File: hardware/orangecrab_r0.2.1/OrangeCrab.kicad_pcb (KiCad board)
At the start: 6 copper layers, 50.8 x 22.9 mm, 96 parts, among them J6 Conn_01x05, U1 TLV62569DRL, U10 NCP115-2.5, U2 TLV62569DRL, U3 LFE5U-25F-8MG285C, U4 MT41K64M16TW-107_J-TR, U6 W25Q128JVP, U7 TLV62569DRL

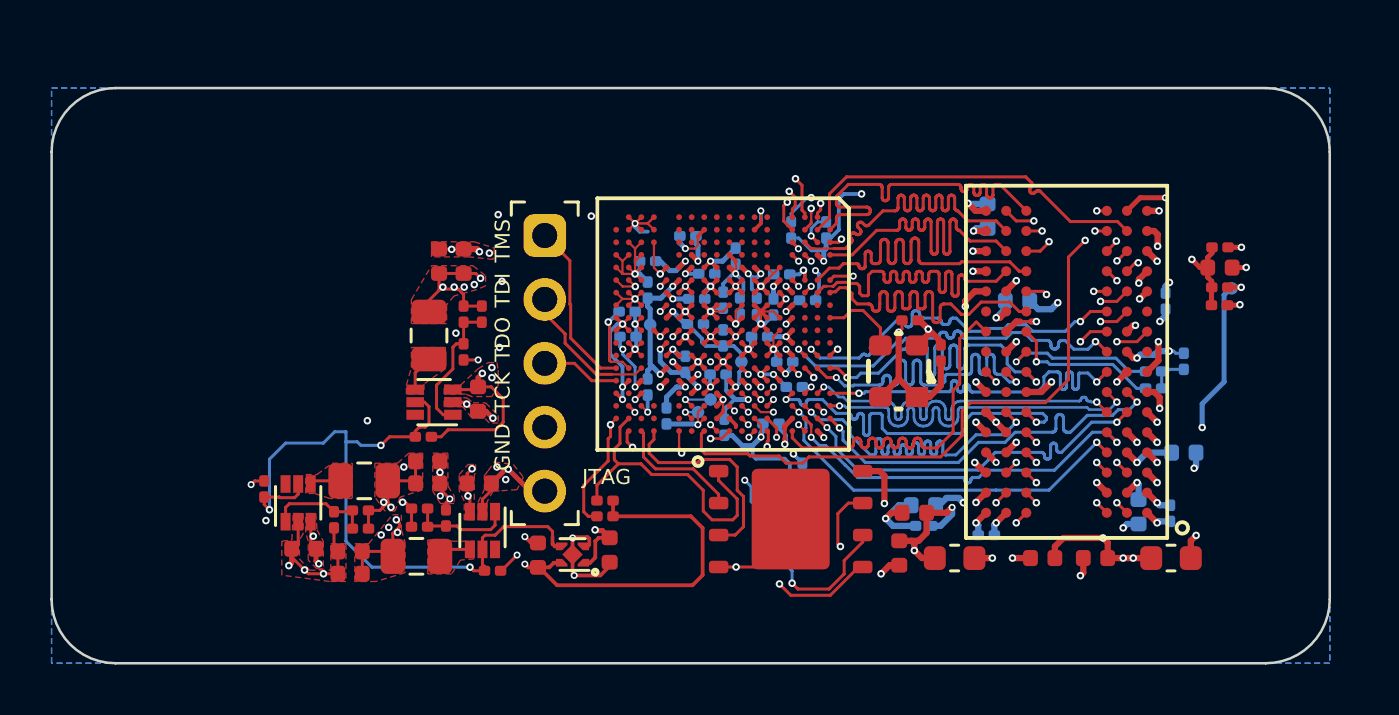
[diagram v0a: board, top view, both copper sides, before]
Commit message: M.2 form factor
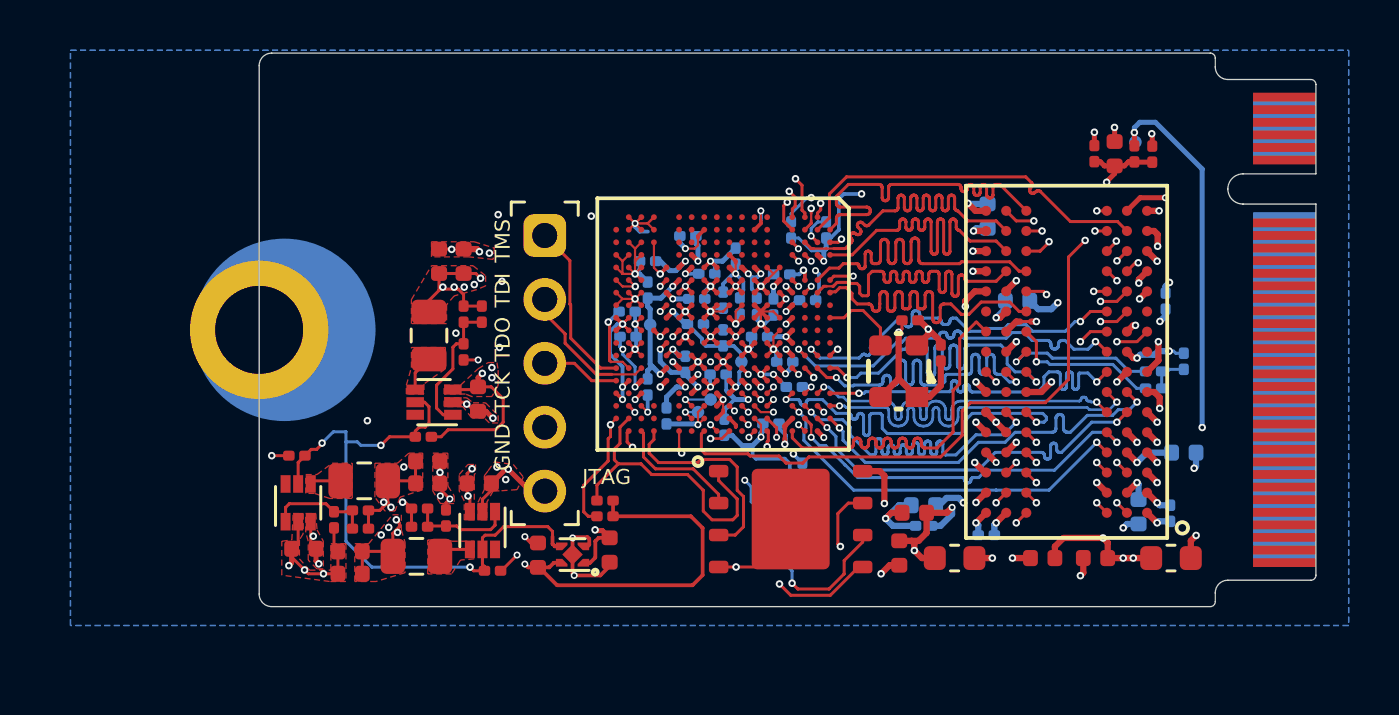
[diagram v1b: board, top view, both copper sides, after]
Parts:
- added U$1: M.2-B-KEY, M.2-Templates:M.2-B-KEY, F.Cu at (184.8, 101.1)
- moved TP31 6.96 mm to (177.6, 93.7), turned to 90 degrees
- moved R2 6.57 mm to (178.3, 94.1), turned to 90 degrees
- moved R1 6.30 mm to (177.5, 94.1), turned to -90 degrees
- moved C2 6.23 mm to (176.0, 94.1), turned to 90 degrees
- moved C3 6.16 mm to (176.8, 94.1), turned to 90 degrees
- moved R25 1.86 mm to (144.3, 106.1), turned to 180 degrees
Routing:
- net P1.35V: track 93.5 -> 101.5 mm
- net EN: track 28.7 -> 24.1 mm
- net VSYS: track 32.6 -> 29.0 mm
- net GND: vias 102 -> 101
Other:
- board size 50.8 x 22.9 mm -> 42 x 22 mm

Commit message: connect all spare IOs to M.2
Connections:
- U$1 pad MOUNTING-HOLE: unconnected-(U$1-MP1-PadMOUNTING-HOLE) -> GND
- U$1 pad P$1: unconnected-(U$1-1-PadP$1) -> GND
- U$1 pad P$10: unconnected-(U$1-10-PadP$10) -> VSYS
- U$1 pad P$11: unconnected-(U$1-11-PadP$11) -> GND
- U$1 pad P$2: unconnected-(U$1-2-PadP$2) -> VSYS
- U$1 pad P$20: unconnected-(U$1-20-PadP$20) -> 3V3_IO0_H4
- U$1 pad P$21: unconnected-(U$1-21-PadP$21) -> 3V3_IO1_G4
- U$1 pad P$22: unconnected-(U$1-22-PadP$22) -> 3V3_IO2_F4
- U$1 pad P$23: unconnected-(U$1-23-PadP$23) -> 3V3_IO3_F3
- U$1 pad P$24: unconnected-(U$1-24-PadP$24) -> 3V3_IO4_H3
- U$1 pad P$25: unconnected-(U$1-25-PadP$25) -> 3V3_IO5_G3
- U$1 pad P$26: unconnected-(U$1-26-PadP$26) -> 3V3_IO6_J3
- U$1 pad P$27: unconnected-(U$1-27-PadP$27) -> 3V3_IO7_H2
- U$1 pad P$28: unconnected-(U$1-28-PadP$28) -> 3V3_IO8_F2
- U$1 pad P$29: unconnected-(U$1-29-PadP$29) -> 3V3_IO9_G1
- U$1 pad P$3: unconnected-(U$1-3-PadP$3) -> GND
- U$1 pad P$30: unconnected-(U$1-30-PadP$30) -> 3V3_IO10_J2
- U$1 pad P$31: unconnected-(U$1-31-PadP$31) -> 3V3_IO11_J1
- U$1 pad P$32: unconnected-(U$1-32-PadP$32) -> 3V3_IO12_F1
- U$1 pad P$33: unconnected-(U$1-33-PadP$33) -> 3V3_IO13_H1
- U$1 pad P$34: unconnected-(U$1-34-PadP$34) -> 3V3_IO14_K4
- U$1 pad P$35: unconnected-(U$1-35-PadP$35) -> 3V3_IO15_L4
- U$1 pad P$36: unconnected-(U$1-36-PadP$36) -> 3V3_IO16_N4
- U$1 pad P$37: unconnected-(U$1-37-PadP$37) -> 3V3_IO17_N3
- U$1 pad P$38: unconnected-(U$1-38-PadP$38) -> 3V3_IO18_M3
- U$1 pad P$39: unconnected-(U$1-39-PadP$39) -> 3V3_IO19_L3
- U$1 pad P$4: unconnected-(U$1-4-PadP$4) -> VSYS
- U$1 pad P$40: unconnected-(U$1-40-PadP$40) -> 3V3_IO20_K3
- U$1 pad P$41: unconnected-(U$1-41-PadP$41) -> 3V3_IO21_K1
- U$1 pad P$42: unconnected-(U$1-42-PadP$42) -> 3V3_IO22_K2
- U$1 pad P$43: unconnected-(U$1-43-PadP$43) -> 3V3_IO23_L1
- U$1 pad P$44: unconnected-(U$1-44-PadP$44) -> 3V3_IO24_M2
- U$1 pad P$45: unconnected-(U$1-45-PadP$45) -> 3V3_IO25_N2
- U$1 pad P$46: unconnected-(U$1-46-PadP$46) -> 3V3_IO26_M1
- U$1 pad P$47: unconnected-(U$1-47-PadP$47) -> 3V3_IO27_N1
- U$1 pad P$48: unconnected-(U$1-48-PadP$48) -> 3V3_IO28_B11
- U$1 pad P$49: unconnected-(U$1-49-PadP$49) -> 3V3_IO29_C11
- U$1 pad P$5: unconnected-(U$1-5-PadP$5) -> GND
- U$1 pad P$50: unconnected-(U$1-50-PadP$50) -> 3V3_IO30_A11
- U$1 pad P$51: unconnected-(U$1-51-PadP$51) -> 3V3_IO31_A10
- U$1 pad P$52: unconnected-(U$1-52-PadP$52) -> 3V3_IO32_B10
- U$1 pad P$53: unconnected-(U$1-53-PadP$53) -> 3V3_IO33_C10
- U$1 pad P$54: unconnected-(U$1-54-PadP$54) -> 3V3_IO34_B9
- U$1 pad P$55: unconnected-(U$1-55-PadP$55) -> 3V3_IO35_C9
- U$1 pad P$56: unconnected-(U$1-56-PadP$56) -> 3V3_IO36_A8
- U$1 pad P$57: unconnected-(U$1-57-PadP$57) -> 3V3_IO37_B8
- U$1 pad P$58: unconnected-(U$1-58-PadP$58) -> 3V3_IO38_C8
- U$1 pad P$59: unconnected-(U$1-59-PadP$59) -> 3V3_IO39_N15
- U$1 pad P$6: unconnected-(U$1-6-PadP$6) -> VSYS
- U$1 pad P$60: unconnected-(U$1-60-PadP$60) -> 3V3_IO40_N16
- U$1 pad P$61: unconnected-(U$1-61-PadP$61) -> 3V3_IO41_N17
- U$1 pad P$62: unconnected-(U$1-62-PadP$62) -> 3V3_IO42_M18
- U$1 pad P$63: unconnected-(U$1-63-PadP$63) -> 3V3_IO43_R17
- U$1 pad P$64: unconnected-(U$1-64-PadP$64) -> 3V3_IO44_T17
- U$1 pad P$65: unconnected-(U$1-65-PadP$65) -> 3V3_IO45_R16
- U$1 pad P$7: unconnected-(U$1-7-PadP$7) -> GND
- U$1 pad P$8: unconnected-(U$1-8-PadP$8) -> VSYS
- U$1 pad P$9: unconnected-(U$1-9-PadP$9) -> GND
- U3 pad A10: unconnected-(U3A-PT27B/PCLKC0_1-PadA10) -> 3V3_IO31_A10
- U3 pad A11: unconnected-(U3A-PT27A/PCLKT0_1-PadA11) -> 3V3_IO30_A11
- U3 pad A8: unconnected-(U3B-PT35B/PCLKC1_0-PadA8) -> 3V3_IO36_A8
- U3 pad B10: unconnected-(U3A-PT29A/PCLKT0_0-PadB10) -> 3V3_IO32_B10
- U3 pad B11: unconnected-(U3A-PT4A-PadB11) -> 3V3_IO28_B11
- U3 pad B8: unconnected-(U3B-PT67A-PadB8) -> 3V3_IO37_B8
- U3 pad B9: unconnected-(U3B-PT33A/PCLKT1_1-PadB9) -> 3V3_IO34_B9
- U3 pad C10: unconnected-(U3A-PT29B/PCLKC0_0-PadC10) -> 3V3_IO33_C10
- U3 pad C11: unconnected-(U3A-PT4B-PadC11) -> 3V3_IO29_C11
- U3 pad C8: unconnected-(U3B-PT67B-PadC8) -> 3V3_IO38_C8
- U3 pad C9: unconnected-(U3B-PT33B/PCLKC1_1-PadC9) -> 3V3_IO35_C9
- U3 pad F1: unconnected-(U3D-PR35C-PadF1) -> 3V3_IO12_F1
- U3 pad F2: unconnected-(U3D-PR32A-PadF2) -> 3V3_IO8_F2
- U3 pad F3: unconnected-(U3D-PR26D/PCLKC3_0-PadF3) -> 3V3_IO3_F3
- U3 pad F4: unconnected-(U3D-PR26C/PCLKT3_0-PadF4) -> 3V3_IO2_F4
- U3 pad G1: unconnected-(U3D-PR32B-PadG1) -> 3V3_IO9_G1
- U3 pad G3: unconnected-(U3D-PR29B-PadG3) -> 3V3_IO5_G3
- U3 pad G4: unconnected-(U3D-PR26B/PCLKC3_1-PadG4) -> 3V3_IO1_G4
- U3 pad H1: unconnected-(U3D-PR35D-PadH1) -> 3V3_IO13_H1
- U3 pad H2: unconnected-(U3D-PR29D-PadH2) -> 3V3_IO7_H2
- U3 pad H3: unconnected-(U3D-PR29A/GR_PCLK3_0-PadH3) -> 3V3_IO4_H3
- U3 pad H4: unconnected-(U3D-PR26A/PCLKT3_1-PadH4) -> 3V3_IO0_H4
- U3 pad J1: unconnected-(U3D-PR35B/VREF1_3-PadJ1) -> 3V3_IO11_J1
- U3 pad J2: unconnected-(U3D-PR35A-PadJ2) -> 3V3_IO10_J2
- U3 pad J3: unconnected-(U3D-PR29C/GR_PCLK3_1-PadJ3) -> 3V3_IO6_J3
- U3 pad K1: unconnected-(U3D-PR41D-PadK1) -> 3V3_IO21_K1
- U3 pad K2: unconnected-(U3D-PR44A-PadK2) -> 3V3_IO22_K2
- U3 pad K3: unconnected-(U3D-PR41C-PadK3) -> 3V3_IO20_K3
- U3 pad K4: unconnected-(U3D-PR38A-PadK4) -> 3V3_IO14_K4
- U3 pad L1: unconnected-(U3D-PR44B-PadL1) -> 3V3_IO23_L1
- U3 pad L3: unconnected-(U3D-PR41B-PadL3) -> 3V3_IO19_L3
- U3 pad L4: unconnected-(U3D-PR38B-PadL4) -> 3V3_IO15_L4
- U3 pad M1: unconnected-(U3D-PR47C/LRC_GPLL0T_IN-PadM1) -> 3V3_IO26_M1
- U3 pad M18: unconnected-(U3G-PB6B/D4/MOSI2/IO4-PadM18) -> 3V3_IO42_M18
- U3 pad M2: unconnected-(U3D-PR44C-PadM2) -> 3V3_IO24_M2
- U3 pad M3: unconnected-(U3D-PR41A-PadM3) -> 3V3_IO18_M3
- U3 pad N1: unconnected-(U3D-PR47D/LRC_GPLL0C_IN-PadN1) -> 3V3_IO27_N1
- U3 pad N15: unconnected-(U3G-PB4A/D7/IO7-PadN15) -> 3V3_IO39_N15
- U3 pad N16: unconnected-(U3G-PB4B/D6/IO6-PadN16) -> 3V3_IO40_N16
- U3 pad N17: unconnected-(U3G-PB6A/D5/MISO2/IO5-PadN17) -> 3V3_IO41_N17
- U3 pad N2: unconnected-(U3D-PR44D-PadN2) -> 3V3_IO25_N2
- U3 pad N3: unconnected-(U3D-PR38D-PadN3) -> 3V3_IO17_N3
- U3 pad N4: unconnected-(U3D-PR38C-PadN4) -> 3V3_IO16_N4
- U3 pad R16: unconnected-(U3G-PB18A/WRITEN-PadR16) -> 3V3_IO45_R16
- U3 pad R17: unconnected-(U3G-PB13A/SN/CSN-PadR17) -> 3V3_IO43_R17
- U3 pad T17: unconnected-(U3G-PB13B/CS1N-PadT17) -> 3V3_IO44_T17

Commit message: Clean up DRC a bit
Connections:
- U$1 pad MOUNTING-HOLE: GND -> unconnected-(U$1-MP1-PadMOUNTING-HOLE)
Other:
- rule pad_to_mask_clearance: 0.03 -> 0
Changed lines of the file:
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@@
   )
   (setup
-    (pad_to_mask_clearance 0.03)
+    (pad_to_mask_clearance 0)
     (pad_to_paste_clearance -0.035)
+    (allow_soldermask_bridges_in_footprints yes)
     (aux_axis_origin 134.51 114.38)
     (grid_origin 134.51 114.38)
@@
   (net 148 "unconnected-(U$1-72-PadP$72)")
   (net 149 "unconnected-(U$1-74-PadP$74)")
+  (net 150 "unconnected-(U$1-MP1-PadMOUNTING-HOLE)")
   (footprint "Package_BGA:BGA-96_9.0x13.0mm_Layout2x3x16_P0.8mm" (layer "F.Cu")
     (at 174.85 102.4 180)
@@
       (stroke (width 0.05) (type solid)) (layer "Edge.Cuts"))
     (pad "MOUNTING-HOLE" thru_hole circle (at 0 -42 90) (size 5.5 5.5) (drill 3.5) (layers "*.Cu" "*.Mask")
-      (net 1 "GND") (pinfunction "MP1") (pintype "bidirectional") (solder_mask_margin 0.1016))
+      (net 150 "unconnected-(U$1-MP1-PadMOUNTING-HOLE)") (pinfunction "MP1") (pintype "bidirectional+no_connect") (solder_mask_margin 0.1016))
     (pad "P$1" smd rect (at 9.25 -1.25 90) (size 0.35 2.5) (layers "F.Cu" "F.Paste" "F.Mask")
       (net 1 "GND") (pinfunction "1") (pintype "bidirectional") (solder_mask_margin 0.1016))

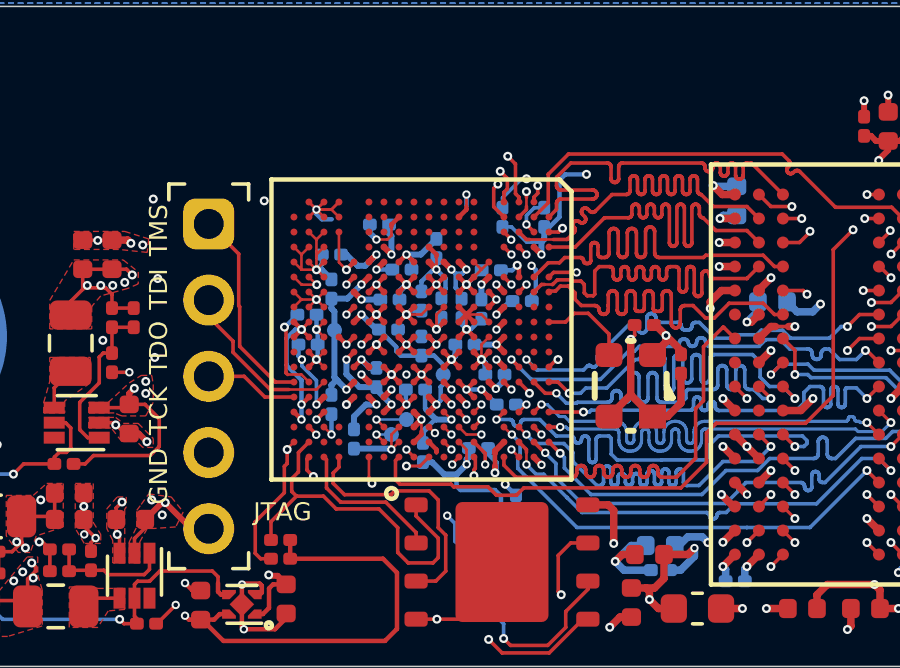
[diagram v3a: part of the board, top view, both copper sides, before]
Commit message: dogbone out all FPGA IOs
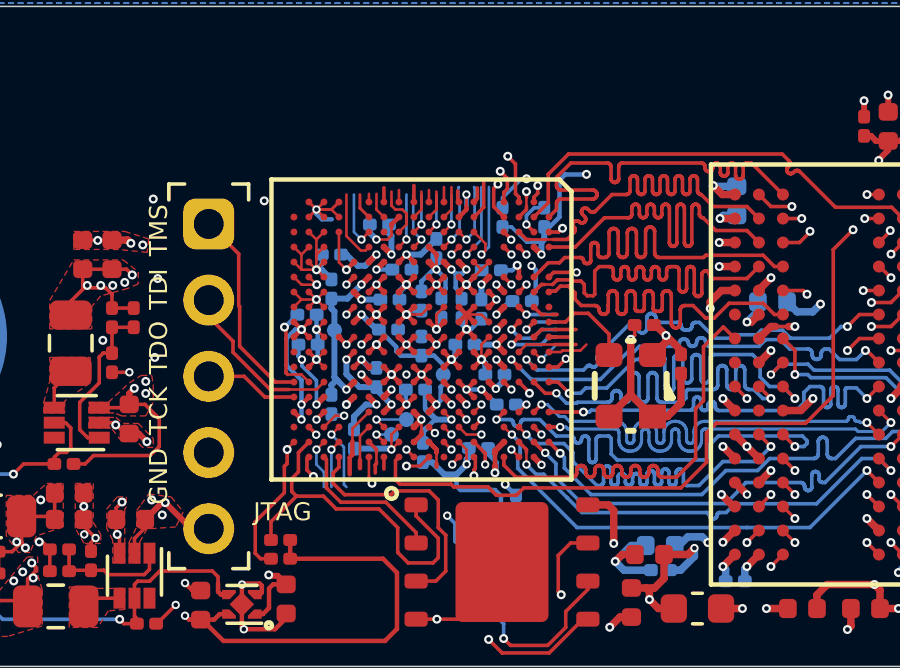
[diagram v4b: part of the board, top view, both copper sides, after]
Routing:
- net 3V3_IO1_G4: track 0.00 -> 11.2 mm, vias 0 -> 1
- net 3V3_IO3_F3: track 0.00 -> 3.32 mm, vias 0 -> 1
- net 3V3_IO2_F4: track 0.00 -> 2.81 mm, vias 0 -> 1
- net 3V3_IO16_N4: track 0.00 -> 2.38 mm
- net 3V3_IO39_N15: track 0.00 -> 2.34 mm
- net 3V3_IO45_R16: track 0.00 -> 2.31 mm, vias 0 -> 1
- net 3V3_IO0_H4: track 0.00 -> 2.25 mm, vias 0 -> 1
- net 3V3_IO5_G3: track 0.00 -> 2.23 mm, vias 0 -> 1
- net 3V3_IO35_C9: track 0.00 -> 2.09 mm, vias 0 -> 1
- net 3V3_IO29_C11: track 0.00 -> 2.01 mm
- net 3V3_IO14_K4: track 0.00 -> 1.98 mm, vias 0 -> 1
- net 3V3_IO17_N3: track 0.00 -> 1.96 mm, vias 0 -> 1
- net 3V3_IO33_C10: track 0.00 -> 1.96 mm, vias 0 -> 1
- net 3V3_IO15_L4: track 0.00 -> 1.86 mm, vias 0 -> 1
- net 3V3_IO19_L3: track 0.00 -> 1.80 mm
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
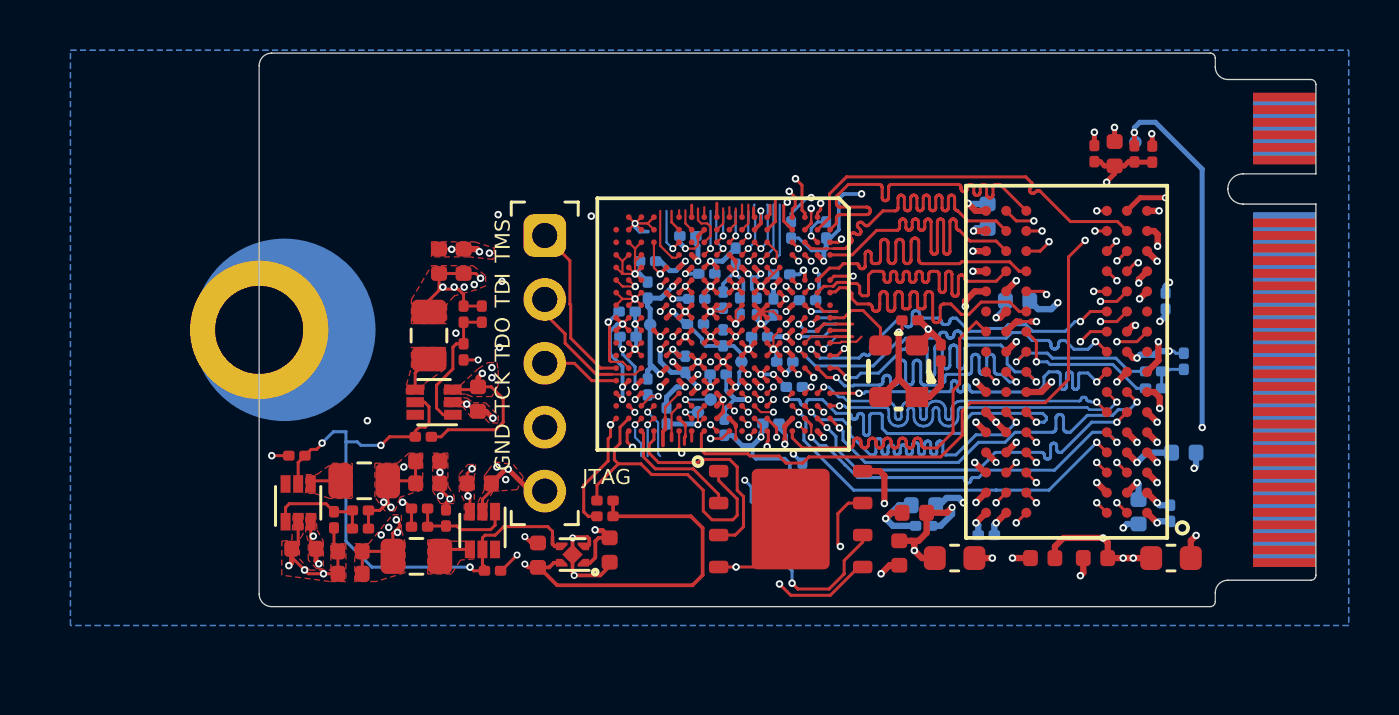
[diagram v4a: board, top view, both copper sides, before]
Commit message: almost finished route bank0 without pinswap
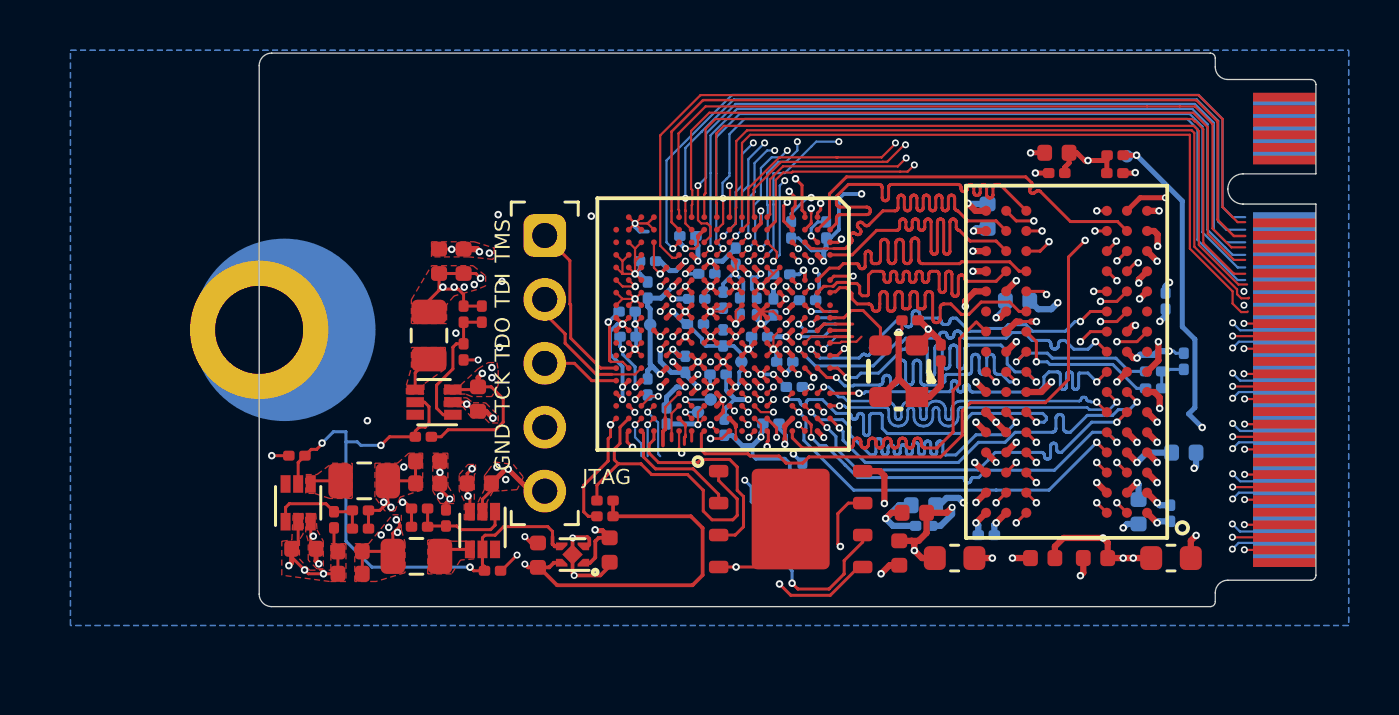
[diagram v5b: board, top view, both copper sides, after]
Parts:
- moved C3 2.30 mm to (174.5, 94.1), turned to 180 degrees
- moved C2 1.68 mm to (174.5, 94.9), turned to 180 degrees
- moved R2 1.67 mm to (176.8, 94.9), turned to 0 degrees
- moved R1 0.77 mm to (176.8, 94.2), turned to 180 degrees
- moved TP31 0.66 mm to (177.2, 94.2), turned to 0 degrees
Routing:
- net 3V3_IO1_G4: track 11.2 -> 44.7 mm, vias 1 -> 2
- net 3V3_IO20_K3: track 1.36 -> 34.3 mm, vias 1 -> 3
- net 3V3_IO27_N1: track 0.28 -> 33.1 mm, vias 0 -> 1
- net 3V3_IO25_N2: track 0.87 -> 33.5 mm, vias 0 -> 1
- net 3V3_IO26_M1: track 0.48 -> 32.9 mm, vias 0 -> 1
- net 3V3_IO19_L3: track 1.80 -> 33.7 mm, vias 0 -> 2
- net 3V3_IO17_N3: track 1.96 -> 33.7 mm, vias 1 -> 2
- net 3V3_IO9_G1: track 0.34 -> 31.6 mm, vias 0 -> 1
- net 3V3_IO7_H2: track 1.10 -> 32.3 mm, vias 0 -> 1
- net 3V3_IO16_N4: track 2.38 -> 33.5 mm
- net 3V3_IO8_F2: track 1.31 -> 32.3 mm, vias 0 -> 1
- net 3V3_IO21_K1: track 0.55 -> 31.4 mm, vias 0 -> 1
- net 3V3_IO12_F1: track 0.52 -> 31.4 mm, vias 0 -> 1
- net 3V3_IO11_J1: track 0.40 -> 31.0 mm, vias 0 -> 2
- net 3V3_IO24_M2: track 0.88 -> 30.9 mm, vias 0 -> 1
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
